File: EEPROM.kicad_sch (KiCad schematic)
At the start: 2 parts, among them U6 24LC256

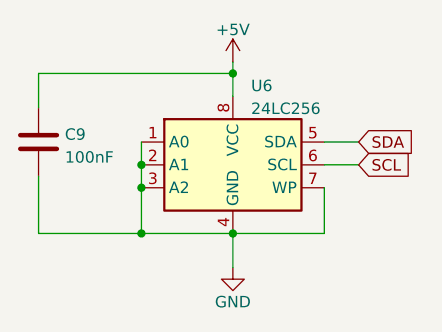
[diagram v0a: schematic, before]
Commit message: redone the switch connectors to accomodate a current sense print. Rearranged parts and updated silk texts to be 50% of their original size
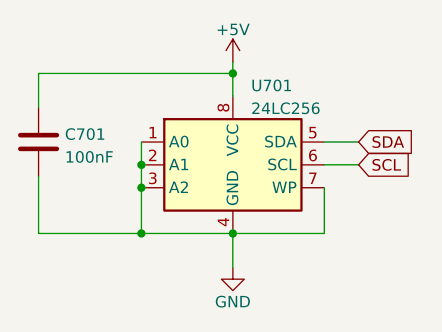
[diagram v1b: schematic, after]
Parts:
- renumbered C9 to C701, U6 to U701
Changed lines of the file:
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@@
   (symbol (lib_id "Device:C") (at 118.11 83.82 0) (unit 1)
     (in_bom yes) (on_board yes) (fields_autoplaced)
-    (property "Reference" "C9" (id 0) (at 121.031 82.9853 0)
+    (property "Reference" "C701" (id 0) (at 121.031 82.9853 0)
       (effects (font (size 1.27 1.27)) (justify left))
     )
@@
   (symbol (lib_id "Memory_EEPROM:24LC256") (at 139.7 86.36 0) (unit 1)
     (in_bom yes) (on_board yes) (fields_autoplaced)
-    (property "Reference" "U6" (id 0) (at 141.7194 77.5802 0)
+    (property "Reference" "U701" (id 0) (at 141.7194 77.5802 0)
       (effects (font (size 1.27 1.27)) (justify left))
     )
@@
   (symbol (lib_id "power:+5V") (at 139.7 74.93 0) (unit 1)
     (in_bom yes) (on_board yes) (fields_autoplaced)
-    (property "Reference" "#PWR0145" (id 0) (at 139.7 78.74 0)
+    (property "Reference" "#PWR0701" (id 0) (at 139.7 78.74 0)
       (effects (font (size 1.27 1.27)) hide)
     )
@@
   (symbol (lib_id "power:GND") (at 139.7 97.79 0) (unit 1)
     (in_bom yes) (on_board yes)
-    (property "Reference" "#PWR0144" (id 0) (at 139.7 104.14 0)
+    (property "Reference" "#PWR0702" (id 0) (at 139.7 104.14 0)
       (effects (font (size 1.27 1.27)) hide)
     )

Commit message: altered the code drastically and made a new PCB. PCB is still much work.
I finally fixed that issue where loco functions and speed were not serviced to the multimaus clients.
The Nx code also has been succesfully tested using the monitor.
MCP bug also has been solded. The bug was in assembleIO.py
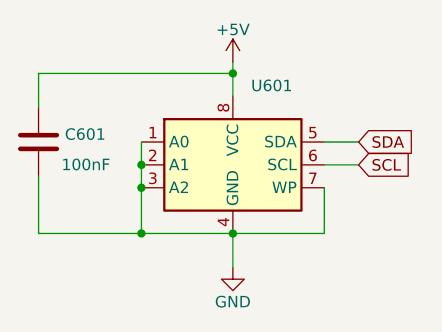
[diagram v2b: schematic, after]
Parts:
- removed C701: 100nF, Capacitor_THT:C_Disc_D3.0mm_W1.6mm_P2.50mm, symbol Device:C
- added C601: 100nF, Capacitor_SMD:C_0603_1608Metric_Pad1.08x0.95mm_HandSolder, symbol Device:C
- U601: renamed from U701; value 24LC256 -> (none); footprint Package_DIP:DIP-8_W7.62mm_Socket -> (none); JCLPCB Part# (none) -> C2987263
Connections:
- net +5V: now also C601.1
- net GND: now also C601.2
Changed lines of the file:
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@@
     )
-  )
-  (symbol (lib_id "Device:C") (at 118.11 83.82 0) (unit 1)
-    (in_bom yes) (on_board yes) (fields_autoplaced)
-    (property "Reference" "C701" (id 0) (at 121.031 82.9853 0)
-      (effects (font (size 1.27 1.27)) (justify left))
-    )
-    (property "Value" "100nF" (id 1) (at 121.031 85.5222 0)
-      (effects (font (size 1.27 1.27)) (justify left))
-    )
-    (property "Footprint" "Capacitor_THT:C_Disc_D3.0mm_W1.6mm_P2.50mm" (id 2) (at 119.0752 87.63 0)
-      (effects (font (size 1.27 1.27)) hide)
-    )
-    (property "Datasheet" "~" (id 3) (at 118.11 83.82 0)
-      (effects (font (size 1.27 1.27)) hide)
-    )
-    (pin "1")
-    (pin "2")
   )
   (symbol (lib_id "Memory_EEPROM:24LC256") (at 139.7 86.36 0) (unit 1)
     (in_bom yes) (on_board yes) (fields_autoplaced)
-    (property "Reference" "U701" (id 0) (at 141.7194 77.5802 0)
+    (property "Reference" "U601" (id 0) (at 141.7194 77.5802 0)
       (effects (font (size 1.27 1.27)) (justify left))
     )
-    (property "Value" "24LC256" (id 1) (at 141.7194 80.1171 0)
+    (property "Value" "" (id 1) (at 141.7194 80.1171 0)
       (effects (font (size 1.27 1.27)) (justify left))
     )
-    (property "Footprint" "Package_DIP:DIP-8_W7.62mm_Socket" (id 2) (at 139.7 86.36 0)
+    (property "Footprint" "" (id 2) (at 139.7 86.36 0)
       (effects (font (size 1.27 1.27)) hide)
     )
     (property "Datasheet" "http://ww1.microchip.com/downloads/en/devicedoc/21203m.pdf" (id 3) (at 139.7 86.36 0)
+      (effects (font (size 1.27 1.27)) hide)
+    )
+    (property "JCLPCB Part#" "C2987263" (id 4) (at 139.7 86.36 0)
       (effects (font (size 1.27 1.27)) hide)
     )
@@
     (pin "8")
   )
+  (symbol (lib_id "Device:C") (at 118.11 83.82 0) (unit 1)
+    (in_bom yes) (on_board yes)
+    (property "Reference" "C601" (id 0) (at 121.031 82.9853 0)
+      (effects (font (size 1.27 1.27)) (justify left))
+    )
+    (property "Value" "100nF" (id 1) (at 120.65 86.36 0)
+      (effects (font (size 1.27 1.27)) (justify left))
+    )
+    (property "Footprint" "Capacitor_SMD:C_0603_1608Metric_Pad1.08x0.95mm_HandSolder" (id 2) (at 119.0752 87.63 0)
+      (effects (font (size 1.27 1.27)) hide)
+    )
+    (property "Datasheet" "~" (id 3) (at 118.11 83.82 0)
+      (effects (font (size 1.27 1.27)) hide)
+    )
+    (property "JLCPCB Part#" "C14663" (id 4) (at 118.11 83.82 0)
+      (effects (font (size 1.27 1.27)) hide)
+    )
+    (pin "1")
+    (pin "2")
+  )
   (symbol (lib_id "power:+5V") (at 139.7 74.93 0) (unit 1)
     (in_bom yes) (on_board yes) (fields_autoplaced)
-    (property "Reference" "#PWR0701" (id 0) (at 139.7 78.74 0)
+    (property "Reference" "#PWR0601" (id 0) (at 139.7 78.74 0)
       (effects (font (size 1.27 1.27)) hide)
     )
@@
   (symbol (lib_id "power:GND") (at 139.7 97.79 0) (unit 1)
     (in_bom yes) (on_board yes)
-    (property "Reference" "#PWR0702" (id 0) (at 139.7 104.14 0)
+    (property "Reference" "#PWR0602" (id 0) (at 139.7 104.14 0)
       (effects (font (size 1.27 1.27)) hide)
     )

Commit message: added missing schematics
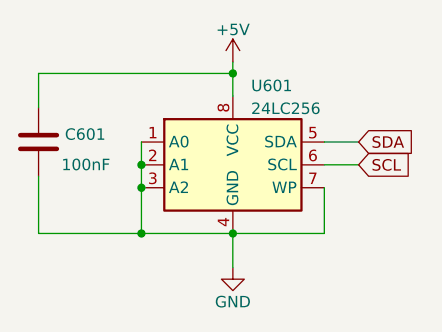
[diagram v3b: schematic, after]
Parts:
- U601: value (none) -> 24LC256; footprint (none) -> Package_SO:SOP-8_3.76x4.96mm_P1.27mm
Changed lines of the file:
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@@
       (effects (font (size 1.27 1.27)) (justify left))
     )
-    (property "Value" "" (id 1) (at 141.7194 80.1171 0)
+    (property "Value" "24LC256" (id 1) (at 141.7194 80.1171 0)
       (effects (font (size 1.27 1.27)) (justify left))
     )
-    (property "Footprint" "" (id 2) (at 139.7 86.36 0)
+    (property "Footprint" "Package_SO:SOP-8_3.76x4.96mm_P1.27mm" (id 2) (at 139.7 86.36 0)
       (effects (font (size 1.27 1.27)) hide)
     )
